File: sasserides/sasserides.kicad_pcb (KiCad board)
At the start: 2 copper layers, 170 x 80 mm, 129 parts, among them J1 Conn_02x16_Odd_Even, Q1 2N7002

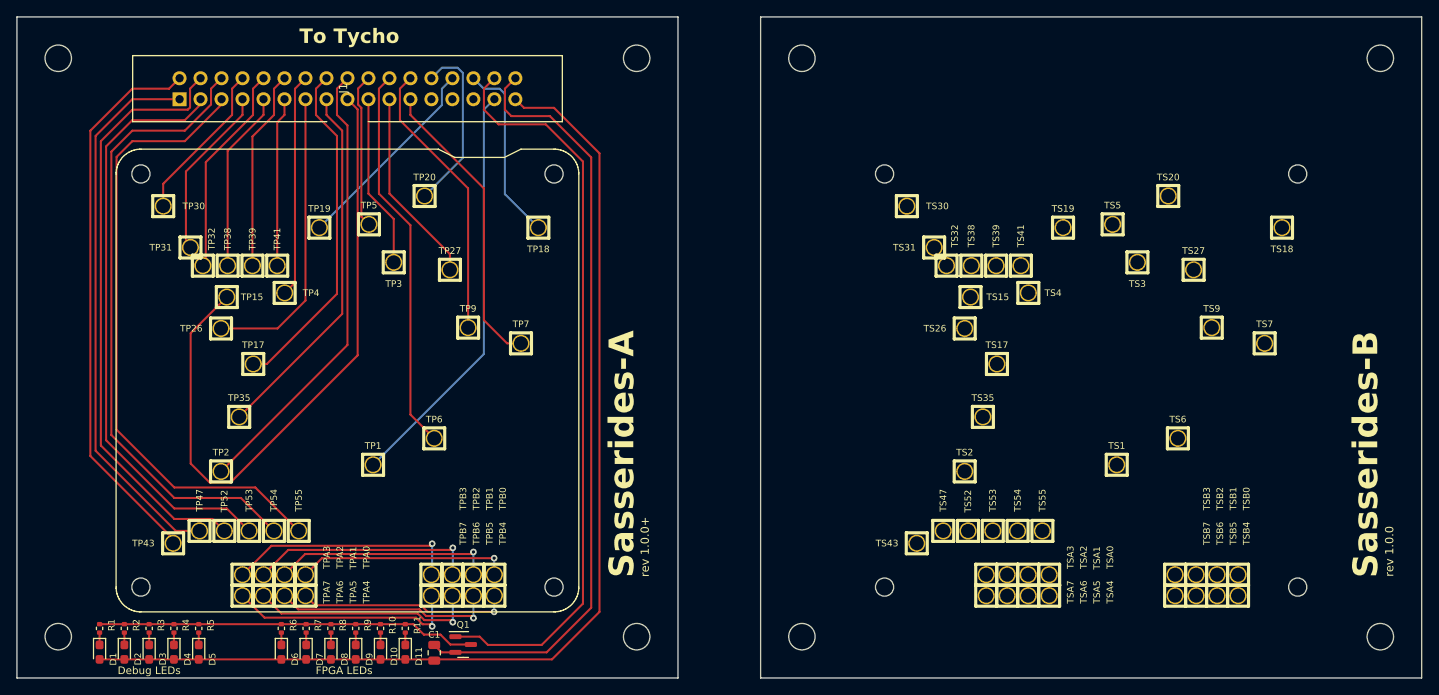
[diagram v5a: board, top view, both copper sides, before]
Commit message: Add clock buffer and revise layout.
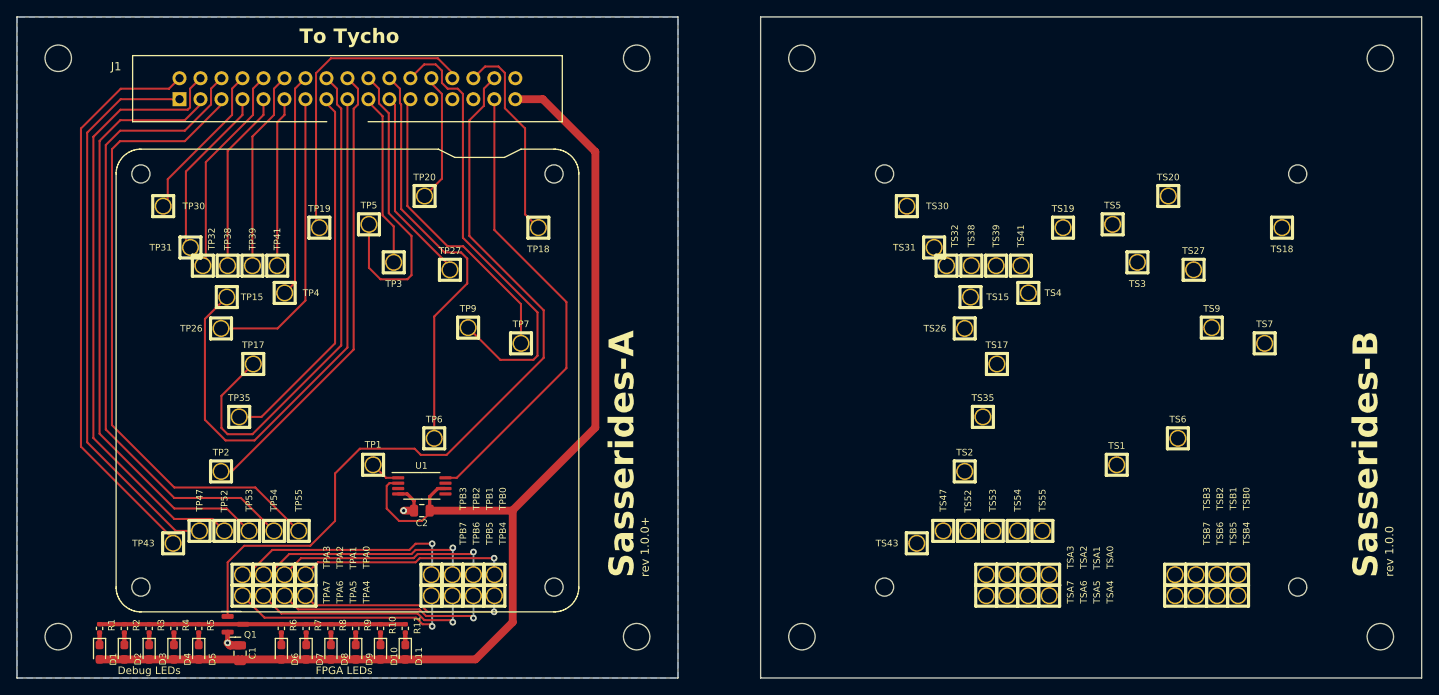
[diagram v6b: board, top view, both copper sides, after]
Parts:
- added C2: 1uF, Capacitor_SMD:C_0805_2012Metric, F.Cu at (109.0, 119.8)
- added U1: CDCV304PW, Package_SO:TSSOP-8_4.4x3mm_P0.65mm, F.Cu at (109.0, 116.8)
- moved Q1 27.7 mm to (86.4, 133.5)
- moved C1 23.5 mm to (87.0, 137.0)
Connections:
- J1 pad 31: /CLK -> /CLK_BUF
- TP1 pad 1: /CLK -> /CLK_EUT
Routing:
- net GND: track 93.3 -> 7.63 mm, vias 0 -> 2
- net /CLK_BUF: track 0.00 -> 56.3 mm
- net /CLK: track 50.3 -> 0.00 mm
- net /TARGET_PHY_3V3: track 34.1 -> 55.0 mm
- net /CONTROL_PHY_1V8: track 41.3 -> 61.7 mm
- net VCC: track 131.3 -> 150.3 mm
- net /+2V5: track 18.7 -> 37.2 mm
- net /MCU_SWDCLK: track 24.8 -> 37.5 mm
- net /~{BTN_PROGRAM}: track 81.0 -> 68.9 mm
- net Net-(Q1-D): track 46.0 -> 37.0 mm
- net REF_LED_EN: track 90.3 -> 97.9 mm
- net /MCU_SWDIO: track 21.4 -> 15.7 mm
- net /CLK_EUT: track 0.00 -> 3.80 mm
- net /VCCRAM: track 46.9 -> 50.3 mm
- net /~{BTN_RESET}: track 22.5 -> 25.1 mm
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- added copper zone on B.Cu, net GND

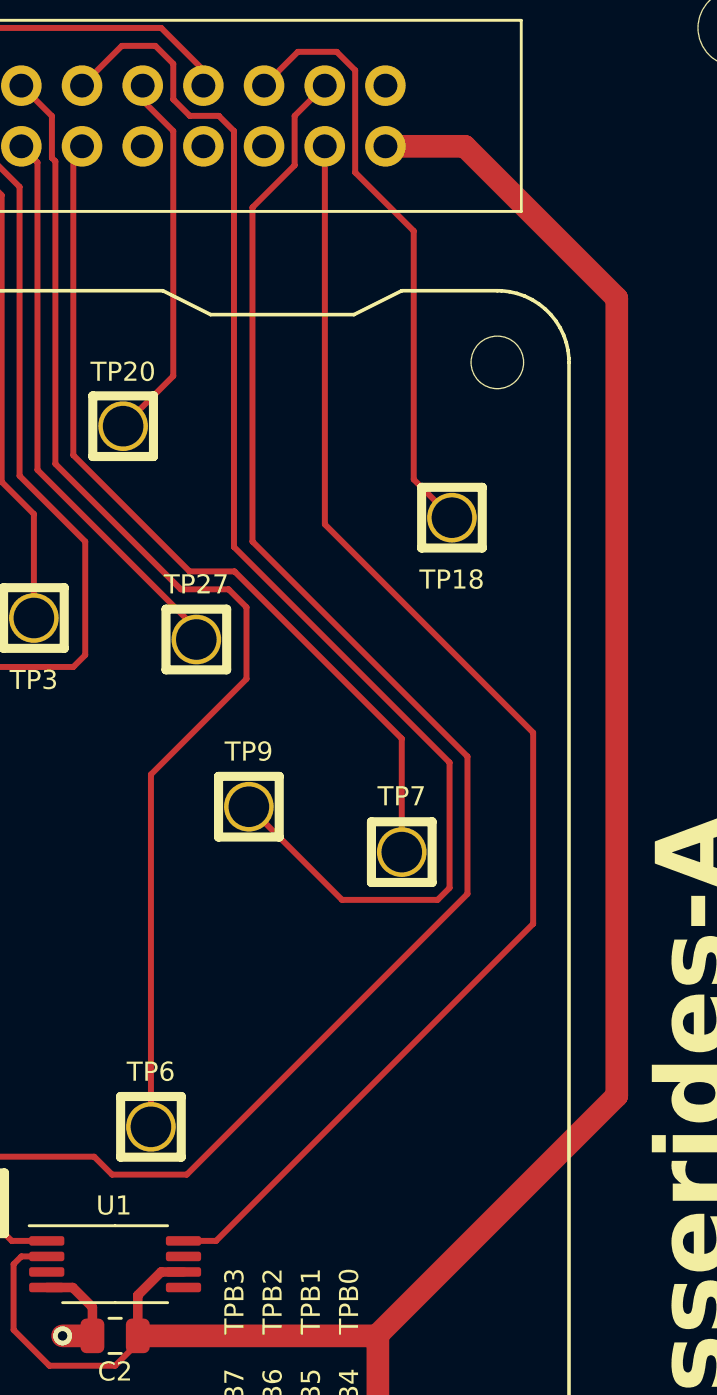
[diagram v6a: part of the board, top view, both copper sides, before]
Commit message: Add zero-ohm series resistor at clock driver.
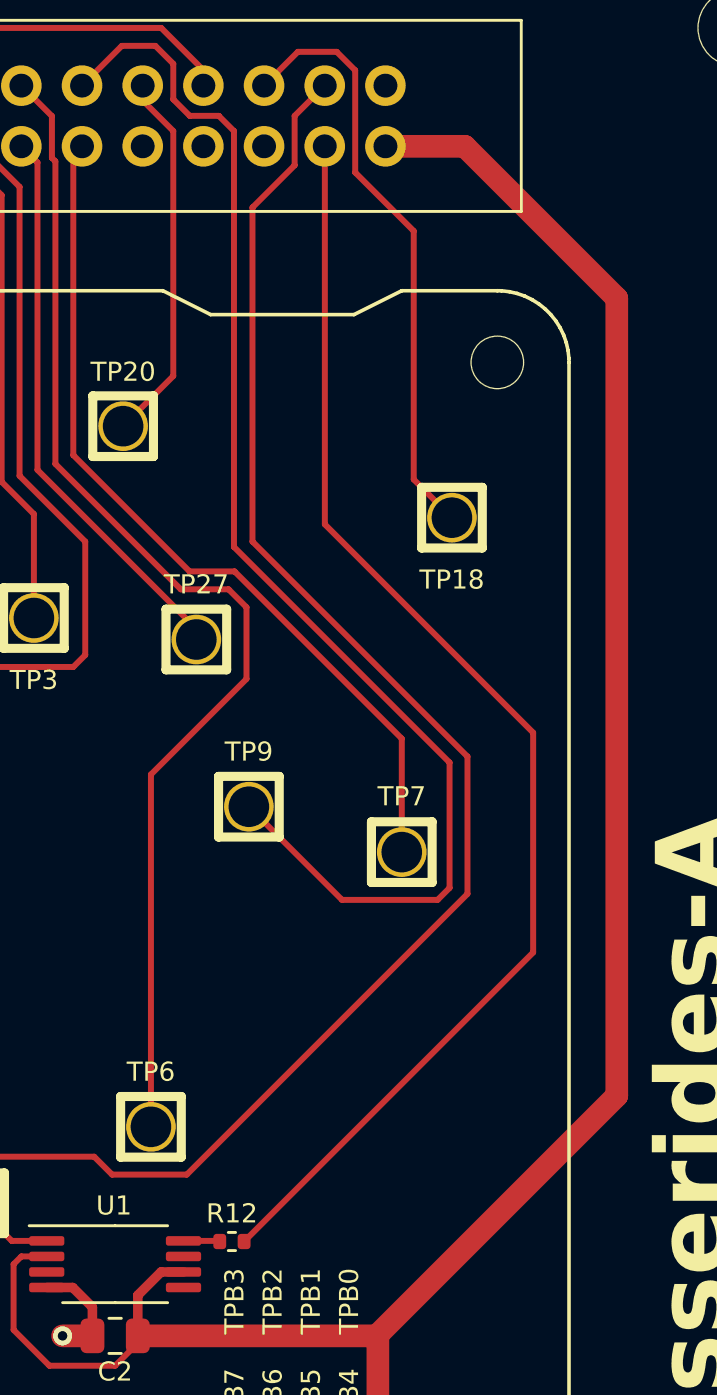
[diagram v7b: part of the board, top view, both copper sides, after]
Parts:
- added R12: 0, Resistor_SMD:R_0402_1005Metric, F.Cu at (113.9, 115.8)
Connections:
- U1 pad 8: /CLK_BUF -> Net-(U1-1Y3)
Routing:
- net /CLK_BUF: track 56.3 -> 54.5 mm
- net Net-(U1-1Y3): track 0.00 -> 1.53 mm
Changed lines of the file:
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@@
   (net 101 "unconnected-(U1-1Y2-Pad7)")
   (net 102 "unconnected-(U1-1Y0-Pad3)")
+  (net 103 "Net-(U1-1Y3)")
   (footprint "MountingHole:MountingHole_2.2mm_M2" (layer "F.Cu")
     (at 165 79)
@@
       (net 101 "unconnected-(U1-1Y2-Pad7)") (pinfunction "1Y2") (pintype "output+no_connect"))
     (pad "8" smd roundrect (at 2.8625 -0.975) (size 1.475 0.4) (layers "F.Cu" "F.Paste" "F.Mask") (roundrect_rratio 0.25)
-      (net 90 "/CLK_BUF") (pinfunction "1Y3") (pintype "output"))
+      (net 103 "Net-(U1-1Y3)") (pinfunction "1Y3") (pintype "output"))
     (model "${KICAD6_3DMODEL_DIR}/Package_SO.3dshapes/TSSOP-8_4.4x3mm_P0.65mm.wrl"
       (offset (xyz 0 0 0))
@@
       (net 85 "unconnected-(TS53-Pad1)") (pinfunction "1") (pintype "passive+no_connect"))
   )
+  (footprint "Resistor_SMD:R_0402_1005Metric" (layer "F.Cu")
+    (at 113.89 115.8)
+    (descr "Resistor SMD 0402 (1005 Metric), square (rectangular) end terminal, IPC_7351 nominal, (Body size source: IPC-SM-782 page 72, https://www.pcb-3d.com/wordpress/wp-content/uploads/ipc-sm-782a_amendment_1_and_2.pdf), generated with kicad-footprint-generator")
+    (tags "resistor")
+    (property "Sheetfile" "sasserides.kicad_sch")
+    (property "Sheetname" "")
+    (property "ki_description" "Resistor")
+    (property "ki_keywords" "R res resistor")
+    (attr smd)
+    (fp_text reference "R12" (at 0 -1.17) (layer "F.SilkS")
+        (effects (font (size 0.8 0.8) (thickness 0.15)))
+    )
+    (fp_text value "0" (at 0 1.17) (layer "F.Fab")
+        (effects (font (size 1 1) (thickness 0.15)))
+    )
+    (fp_text user "${REFERENCE}" (at 0 0) (layer "F.Fab")
+        (effects (font (size 0.26 0.26) (thickness 0.04)))
+    )
+    (fp_line (start -0.153641 -0.38) (end 0.153641 -0.38)
+      (stroke (width 0.12) (type solid)) (layer "F.SilkS"))
+    (fp_line (start -0.153641 0.38) (end 0.153641 0.38)
+      (stroke (width 0.12) (type solid)) (layer "F.SilkS"))
+    (fp_line (start -0.93 -0.47) (end 0.93 -0.47)
+      (stroke (width 0.05) (type solid)) (layer "F.CrtYd"))
+    (fp_line (start -0.93 0.47) (end -0.93 -0.47)
+      (stroke (width 0.05) (type solid)) (layer "F.CrtYd"))
+    (fp_line (start 0.93 -0.47) (end 0.93 0.47)
+      (stroke (width 0.05) (type solid)) (layer "F.CrtYd"))
+    (fp_line (start 0.93 0.47) (end -0.93 0.47)
+      (stroke (width 0.05) (type solid)) (layer "F.CrtYd"))
+    (fp_line (start -0.525 -0.27) (end 0.525 -0.27)
+      (stroke (width 0.1) (type solid)) (layer "F.Fab"))
+    (fp_line (start -0.525 0.27) (end -0.525 -0.27)
+      (stroke (width 0.1) (type solid)) (layer "F.Fab"))
+    (fp_line (start 0.525 -0.27) (end 0.525 0.27)
+      (stroke (width 0.1) (type solid)) (layer "F.Fab"))
+    (fp_line (start 0.525 0.27) (end -0.525 0.27)
+      (stroke (width 0.1) (type solid)) (layer "F.Fab"))
+    (pad "1" smd roundrect (at -0.51 0) (size 0.54 0.64) (layers "F.Cu" "F.Paste" "F.Mask") (roundrect_rratio 0.25)
+      (net 103 "Net-(U1-1Y3)") (pintype "passive"))
+    (pad "2" smd roundrect (at 0.51 0) (size 0.54 0.64) (layers "F.Cu" "F.Paste" "F.Mask") (roundrect_rratio 0.25)
+      (net 90 "/CLK_BUF") (pintype "passive"))
+    (model "${KICAD6_3DMODEL_DIR}/Resistor_SMD.3dshapes/R_0402_1005Metric.wrl"
+      (offset (xyz 0 0 0))
+      (scale (xyz 1 1 1))
+      (rotate (xyz 0 0 0))
+    )
+  )
   (footprint "tycho:HEADER-1x1-TESTPROBE" (layer "F.Cu")
     (at 182.38 127.5)
@@
   (segment (start 119.05 71.05) (end 121.5 73.5) (width 0.25) (layer "F.Cu") (net 89))
   (segment (start 119.05 66.775) (end 119.05 71.05) (width 0.25) (layer "F.Cu") (net 89))
-  (segment (start 117.78 85.78) (end 126.5 94.5) (width 0.25) (layer "F.Cu") (net 90))
-  (segment (start 117.78 69.955) (end 117.78 85.78) (width 0.25) (layer "F.Cu") (net 90))
-  (segment (start 126.5 94.5) (end 126.5 102.5) (width 0.25) (layer "F.Cu") (net 90))
-  (segment (start 126.5 102.5) (end 113.225 115.775) (width 0.25) (layer "F.Cu") (net 90))
-  (segment (start 113.225 115.775) (end 111.8625 115.775) (width 0.25) (layer "F.Cu") (net 90))
+  (segment (start 117.78 85.78) (end 117.78 69.955) (width 0.25) (layer "F.Cu") (net 90))
+  (segment (start 126.5 94.5) (end 117.78 85.78) (width 0.25) (layer "F.Cu") (net 90))
+  (segment (start 114.4 115.8) (end 126.5 103.7) (width 0.25) (layer "F.Cu") (net 90))
+  (segment (start 126.5 103.7) (end 126.5 94.5) (width 0.25) (layer "F.Cu") (net 90))
   (segment (start 94.92 127.5) (end 96.42 126) (width 0.25) (layer "F.Cu") (net 91))
   (segment (start 108.25 126) (end 108.75 125.5) (width 0.25) (layer "F.Cu") (net 91))
@@
   (segment (start 104.675 115.775) (end 103.1 114.2) (width 0.25) (layer "F.Cu") (net 99))
   (segment (start 106.1375 115.775) (end 104.675 115.775) (width 0.25) (layer "F.Cu") (net 99))
+  (segment (start 113.355 115.775) (end 113.38 115.8) (width 0.25) (layer "F.Cu") (net 103))
+  (segment (start 111.8625 115.775) (end 113.355 115.775) (width 0.25) (layer "F.Cu") (net 103))
   (zone (net 0) (net_name "") (layers "F&B.Cu") (hatch edge 0.5)
     (connect_pads yes (clearance 0))

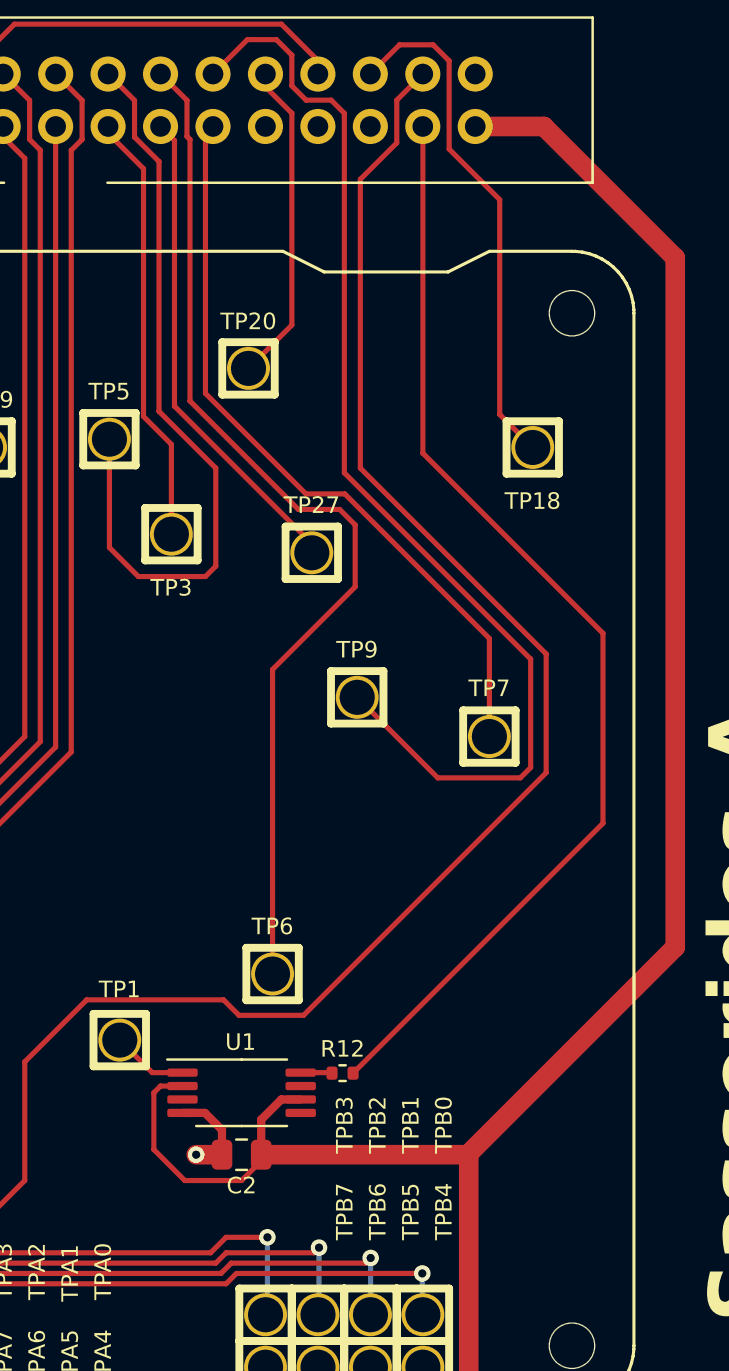
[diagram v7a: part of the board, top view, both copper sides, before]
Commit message: Add a 1M pulldown resistor at clock buffer input.
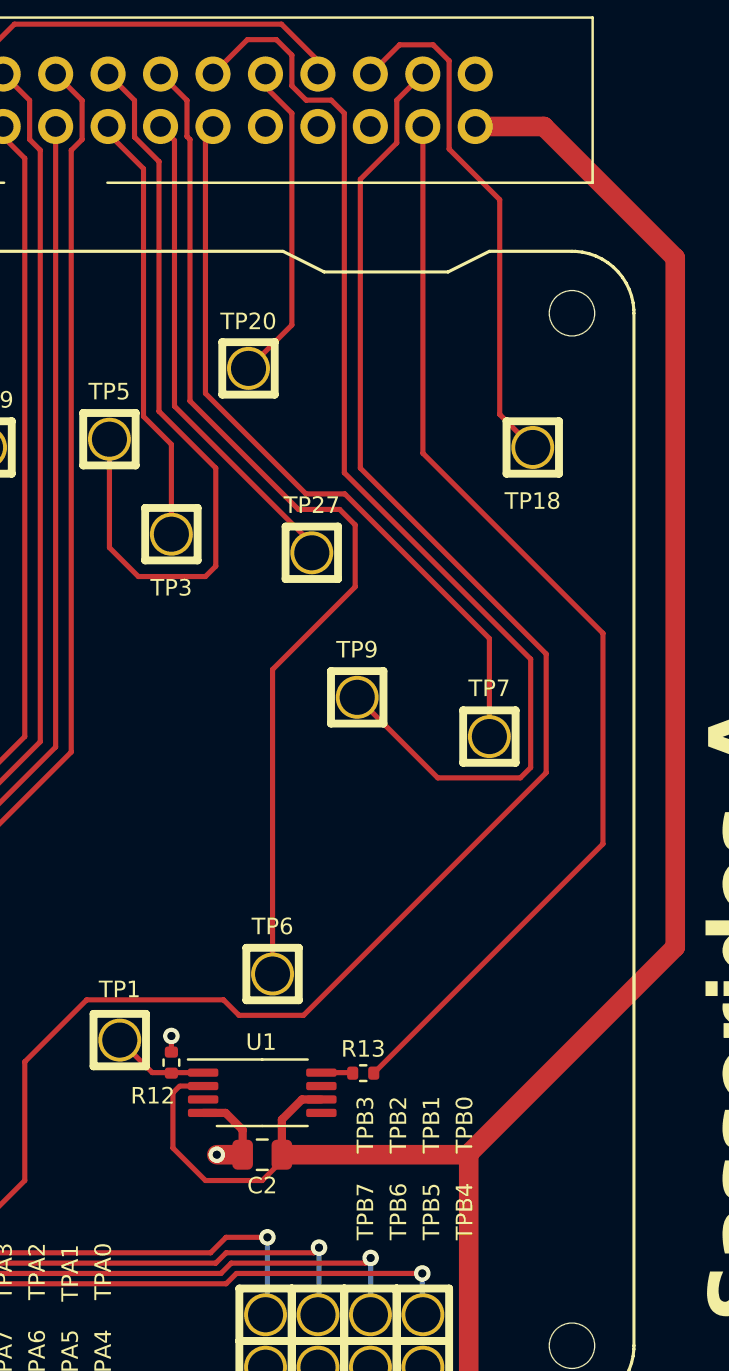
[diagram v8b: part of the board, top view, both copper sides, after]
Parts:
- added R12: 1M, Resistor_SMD:R_0402_1005Metric, F.Cu at (105.6, 115.3)
- moved C2 1.00 mm to (110.0, 119.8)
- moved R13 1.00 mm to (114.9, 115.8)
- moved U1 1.00 mm to (110.0, 116.8)
- renumbered R12 to R13
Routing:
- net /CLK_EUT: track 3.80 -> 4.82 mm
- net VCC: track 150.3 -> 149.4 mm
- net GND: track 7.63 -> 8.41 mm, vias 2 -> 3
